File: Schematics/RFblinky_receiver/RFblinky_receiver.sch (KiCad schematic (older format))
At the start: 19 parts, among them U1 LT1117-3.3, U2 L7805, U3 MSP430G2231IN14, U4 SMAKN-433RX

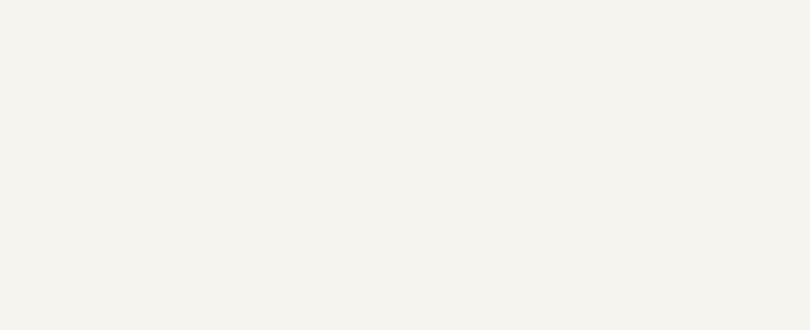
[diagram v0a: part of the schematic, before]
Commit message: Created schematic pdfs, added README, commented ReceiverModule
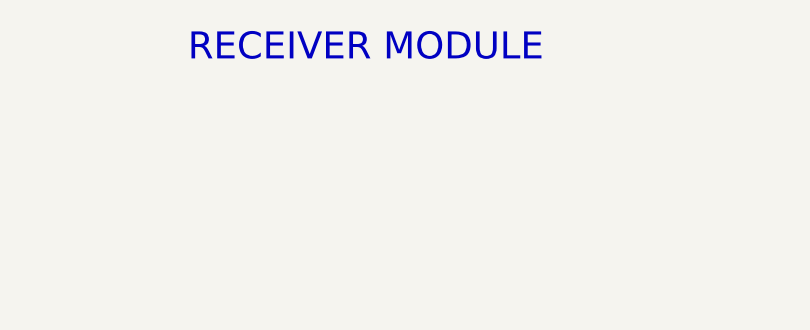
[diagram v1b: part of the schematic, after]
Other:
- note added: "RECEIVER MODULE"
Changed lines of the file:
@@
 Text Notes 6050 2150 0    50   ~ 0
 MCU
+Text Notes 5000 900  0    118  ~ 0
+RECEIVER MODULE
 $EndSCHEMATC
